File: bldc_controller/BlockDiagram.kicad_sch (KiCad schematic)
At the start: 0 parts

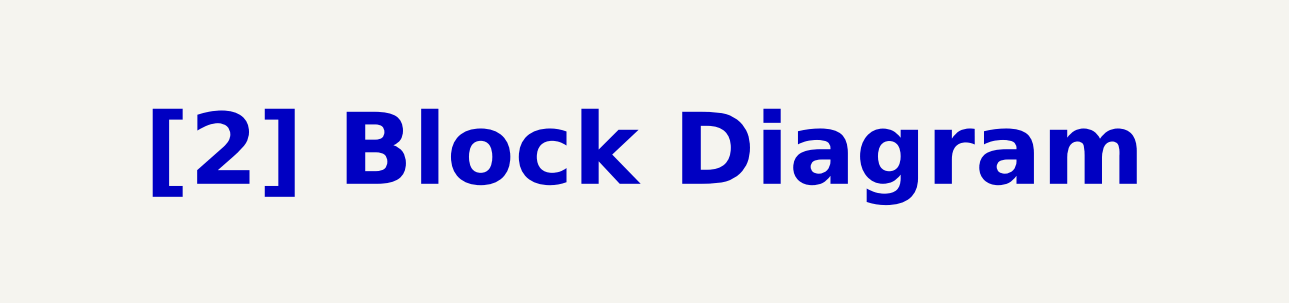
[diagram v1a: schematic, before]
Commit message: Replaced 3v3 buck with WSON package alternative. Will back-annotate components
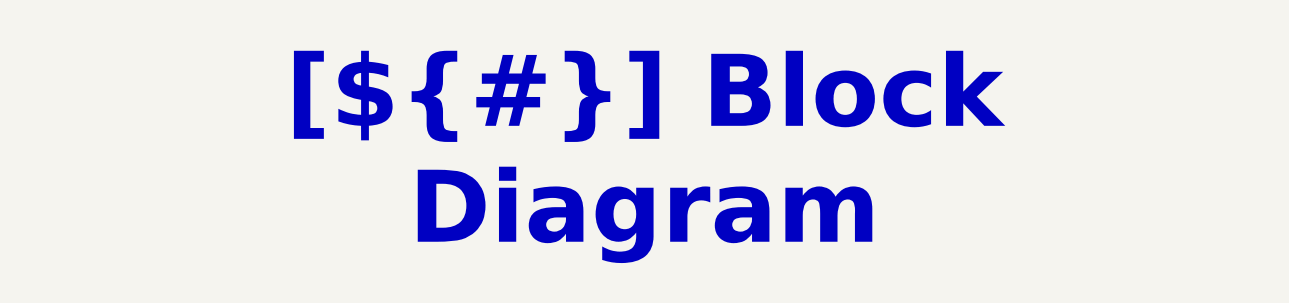
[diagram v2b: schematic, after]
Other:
- company: (none) -> ${COMPANY}
- title: (none) -> Block Diagram
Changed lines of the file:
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@@
 (kicad_sch (version 20230121) (generator eeschema)
   (paper "A3")
-  (text_box "[2] Block Diagram"
+  (title_block
+    (title "Block Diagram")
+    (date "2023-11-30")
+    (rev "${REVISION}")
+    (company "${COMPANY}")
+    (comment 3 "Author: ${AUTHOR}")
+  )
+  (text_box "[${#}] ${TITLE}"
     (at 144.78 20.32 0) (size 130.81 12.7)
     (stroke (width -0.0001) (type default))

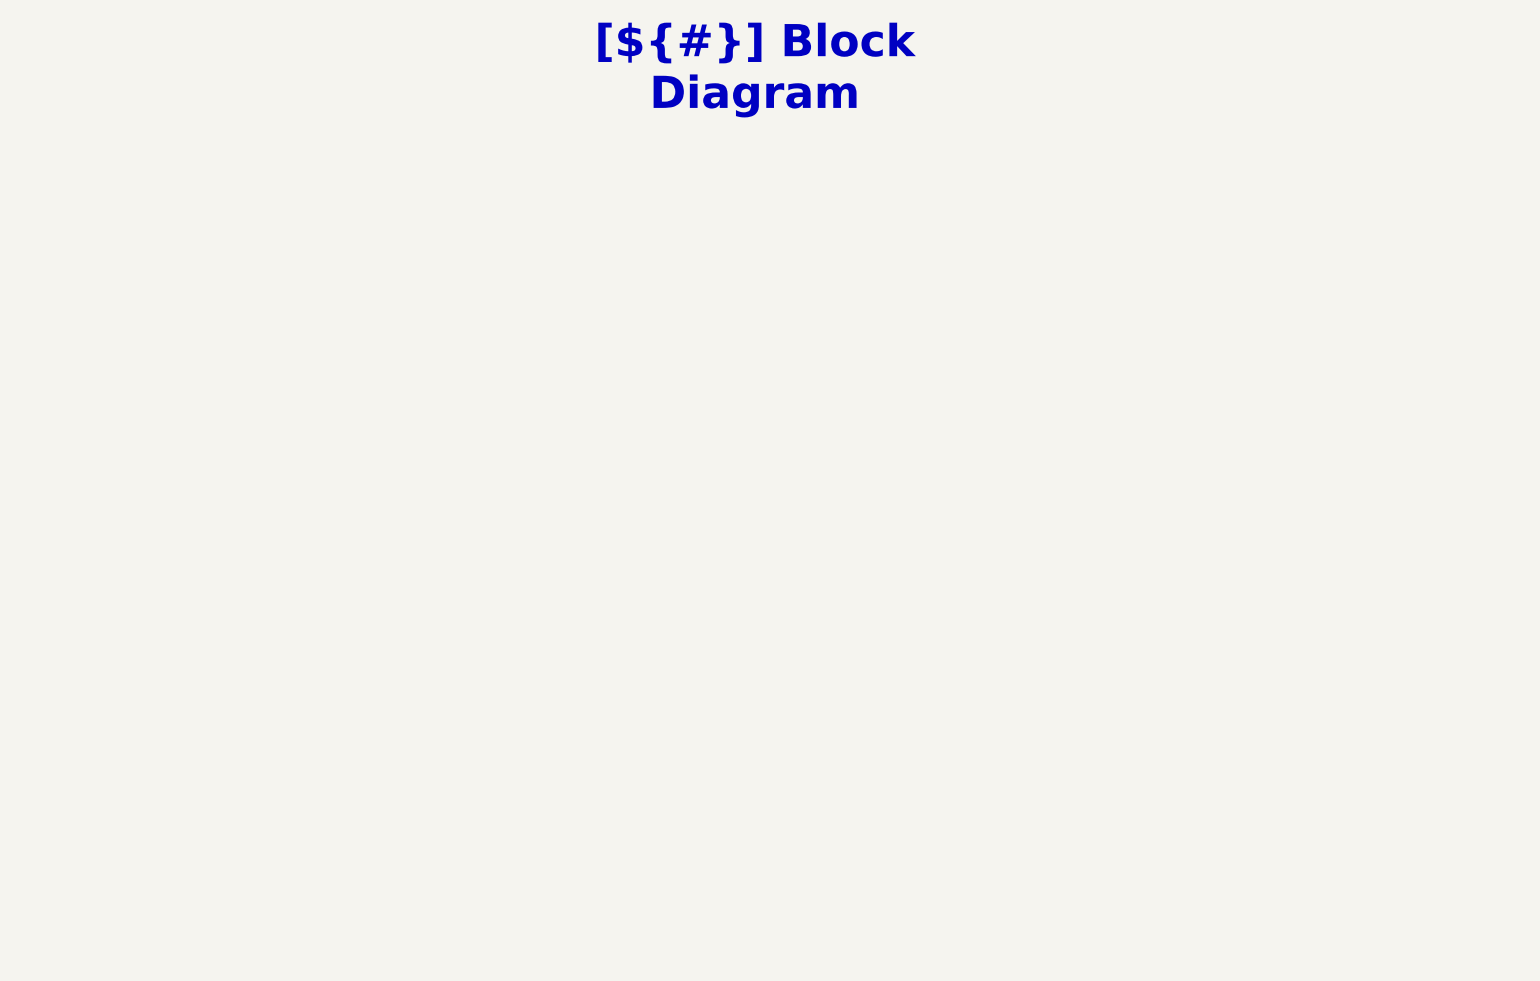
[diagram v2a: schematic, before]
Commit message: Added block diagram, currently rerouting power polygons
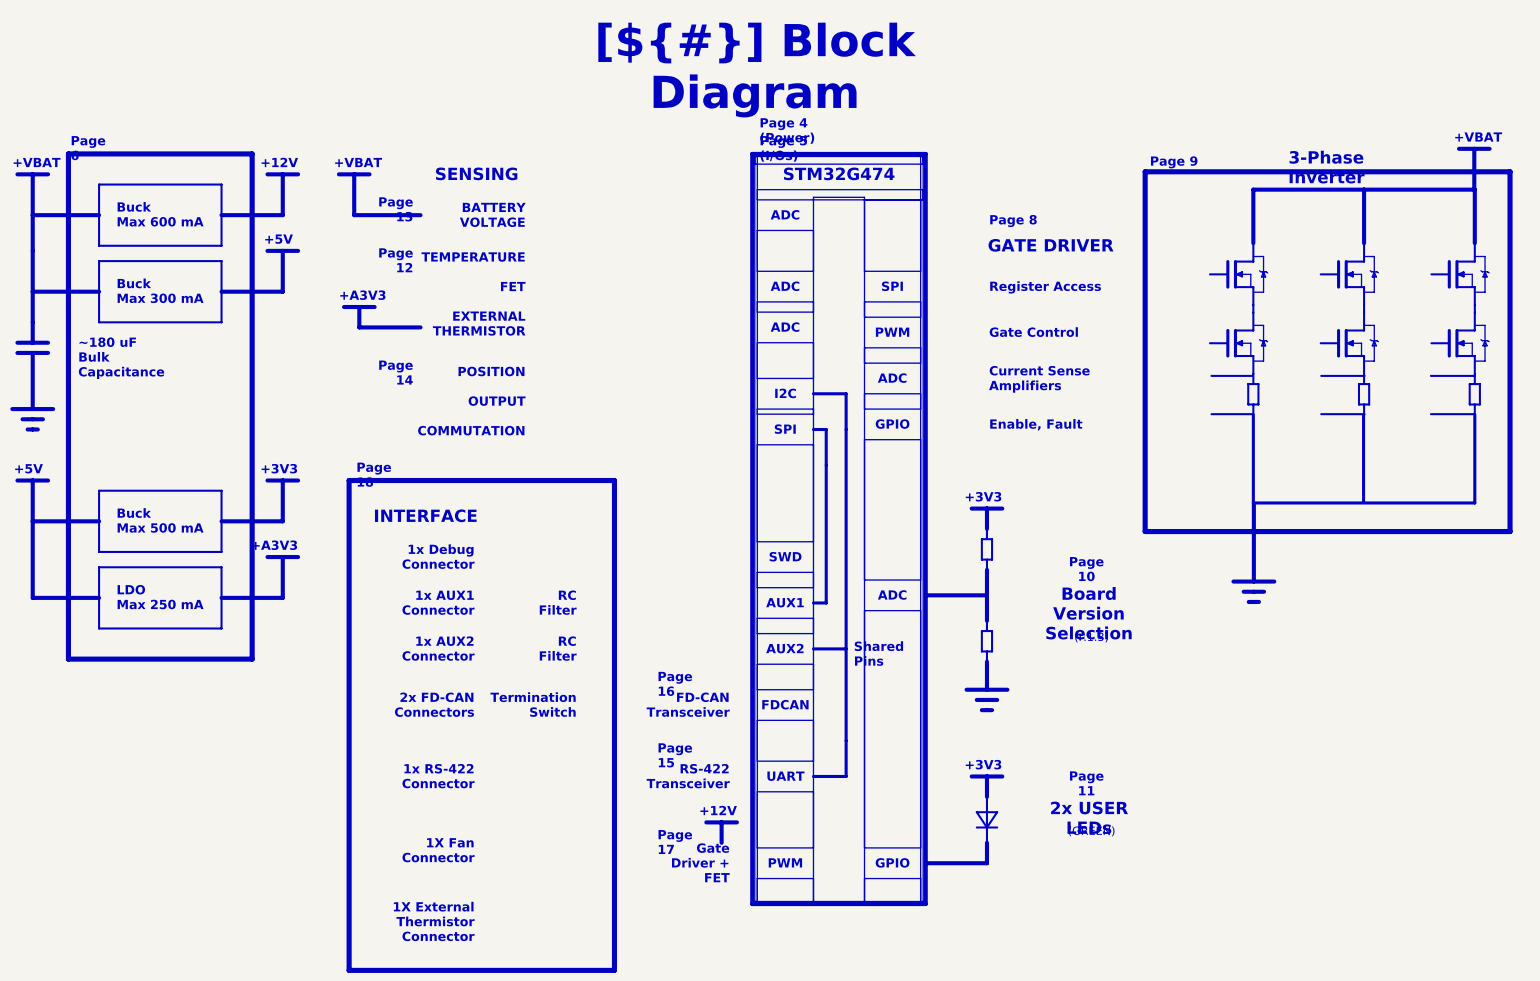
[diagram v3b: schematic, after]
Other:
- note added: "+12V"
- note added: "+3V3"
- note added: "+5V"
- note added: "+A3V3"
- note added: "+VBAT"

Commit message: finished most of routing. Need to add testpoints and clean up graphics
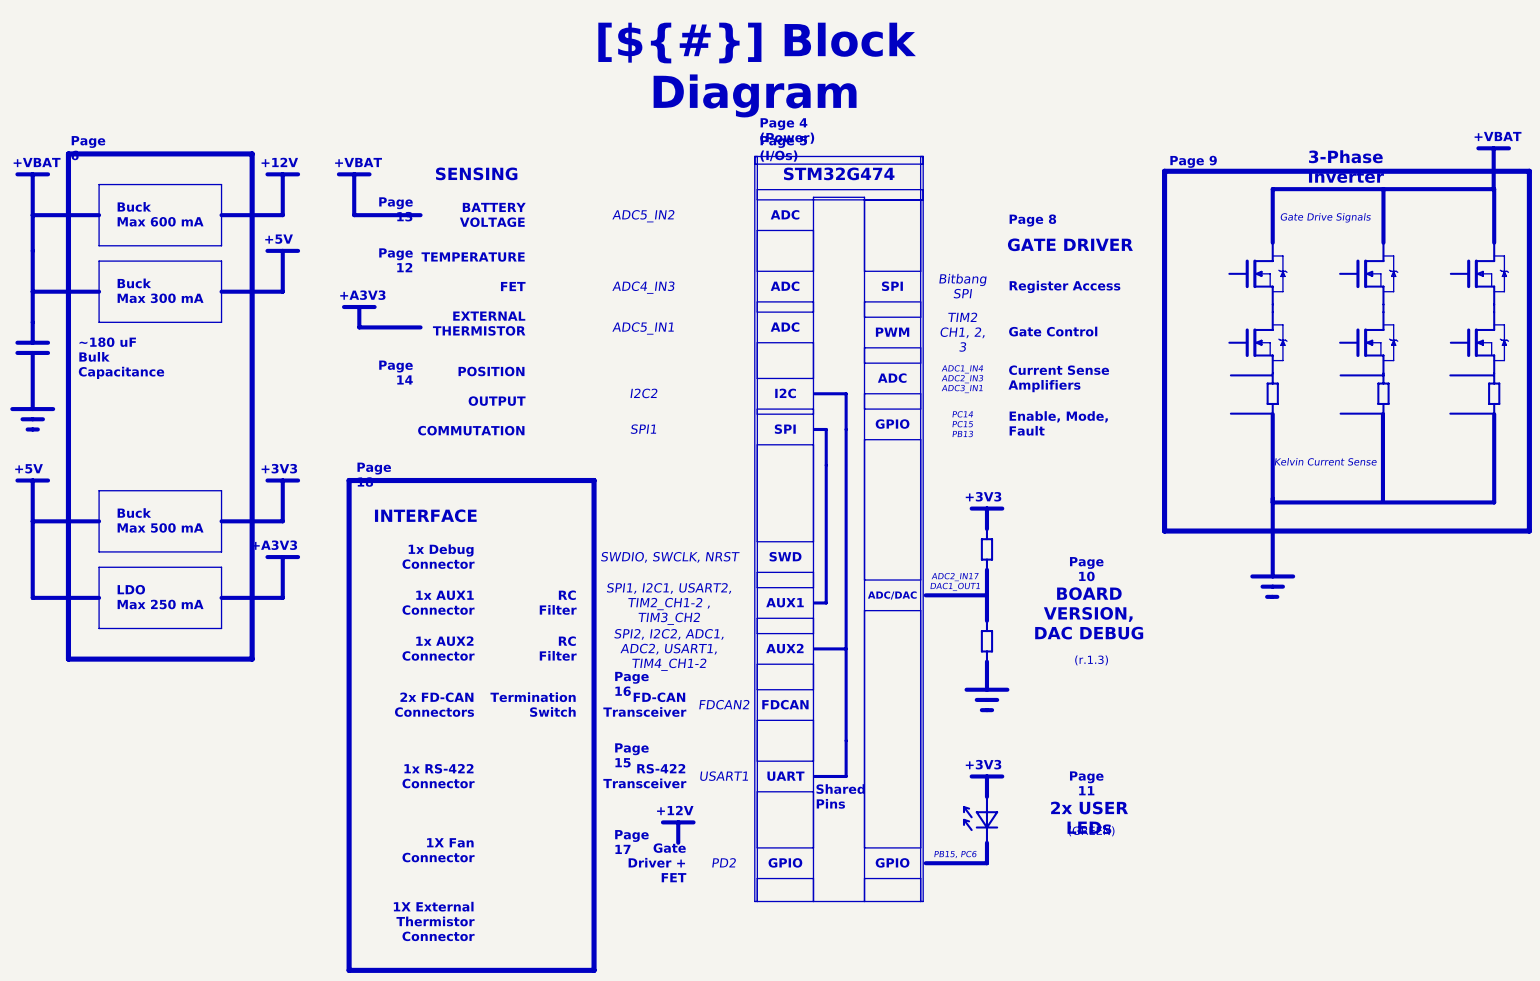
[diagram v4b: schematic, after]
